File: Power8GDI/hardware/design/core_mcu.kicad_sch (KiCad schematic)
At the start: 31 parts, among them J101 SWD 3V3 target reference, U101 STM32F767IIT6, Y101 ASEM1-8.000MHZ-LC-T

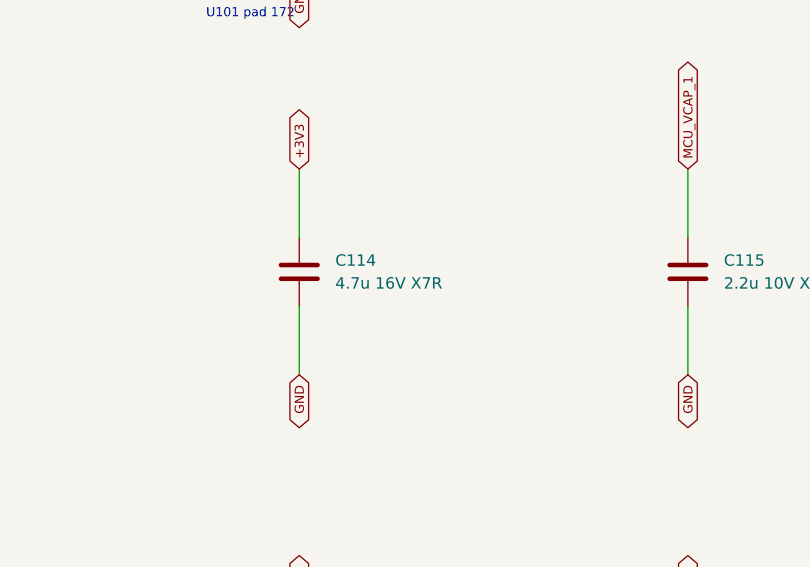
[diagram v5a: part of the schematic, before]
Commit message: Review B58 injector power stage and bind selected GDI6 BOM
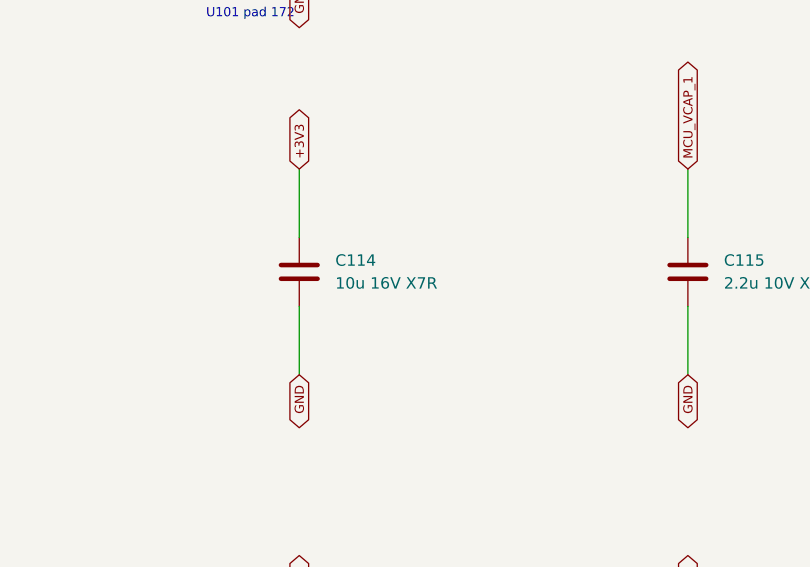
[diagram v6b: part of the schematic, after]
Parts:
- C101, C102, C103, C104, C105, C106, C107, C108, C109, C110, C111, C112, C113, C117, C119, C121, C123, C124: Hardware_Qualification (none) -> BOARD_QUALIFICATION_PENDING; MPN (none) -> C0603C104K5RACTU; Manufacturer (none) -> KEMET; Procurement_Status (none) -> SELECTED_CATALOG_ITEM; Purchase_Released (none) -> false; Selection_Gaps (none) -> []; Selection_ID (none) -> SEL-6bf9727c4e40; Selection_Ratings (none) -> {"capacitance_pf": 100000, "dielectric": "X7R", "rated_volt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; Selection_Source_URLs (none) -> https://search.kemet.com/download/specsheet/C0603C104K5RACTU
- C114: value 4.7u 16V X7R -> 10u 16V X7R; footprint Capacitor_SMD:C_0603_1608Metric -> Capacitor_SMD:C_1206_3216Metric; Design note Package bulk; effective capacitance >=4.7uF after bias/temp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 -> C1206C106K4RACTU candidate; >=4.7uF effective remains a qua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; Hardware_Qualification (none) -> EFFECTIVE_CAPACITANCE_VALIDATION_REQUIRED; MPN (none) -> C1206C106K4RACTU; Manufacturer (none) -> KEMET; Procurement_Status (none) -> SELECTED_CONDITIONAL; Purchase_Released (none) -> false; Selection_Gaps (none) -> ["Nominal10uF alone does not establish required4.7uF effect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; Selection_ID (none) -> SEL-1d8e2bf57acc; Selection_Ratings (none) -> {"capacitance_pf": 10000000, "dc_bias_qualification": "PEND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; Selection_Source_URLs (none) -> https://search.kemet.com/component-documentation/download/s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
- C115, C116: Hardware_Qualification (none) -> BOARD_QUALIFICATION_PENDING; MPN (none) -> C0603C225K8RACTU; Manufacturer (none) -> KEMET; Procurement_Status (none) -> SELECTED_CATALOG_ITEM; Purchase_Released (none) -> false; Selection_Gaps (none) -> ["Required effective capacitance not yet verified with supp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; Selection_ID (none) -> SEL-6e8be3f03886; Selection_Ratings (none) -> {"capacitance_pf": 2200000, "dc_bias_qualification": "PENDI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; Selection_Source_URLs (none) -> https://www.tme.com/us/en-us/details/c0603c225k8rac/mlcc-sm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
- C118, C120, C122: Hardware_Qualification (none) -> BOARD_QUALIFICATION_PENDING; MPN (none) -> C0603C105K3RACTU; Manufacturer (none) -> KEMET; Procurement_Status (none) -> SELECTED_CATALOG_ITEM; Purchase_Released (none) -> false; Selection_Gaps (none) -> []; Selection_ID (none) -> SEL-4bca20b134b8; Selection_Ratings (none) -> {"capacitance_pf": 1000000, "dc_bias_qualification": "PENDI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; Selection_Source_URLs (none) -> https://search.kemet.com/download/specsheet/C0603C105K3RACTU
- C129: Hardware_Qualification (none) -> BOARD_QUALIFICATION_PENDING; MPN (none) -> C0603C103K5RACTU; Manufacturer (none) -> KEMET; Procurement_Status (none) -> SELECTED_CATALOG_ITEM; Purchase_Released (none) -> false; Selection_Gaps (none) -> []; Selection_ID (none) -> SEL-003cf16db818; Selection_Ratings (none) -> {"capacitance_pf": 10000, "dielectric": "X7R", "rated_volta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; Selection_Source_URLs (none) -> https://www.digikey.com/en/products/detail/kemet/C0603C103K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
- J101: Hardware_Qualification (none) -> BOARD_QUALIFICATION_PENDING; MPN (none) -> M50-3500542; Manufacturer (none) -> Harwin; Procurement_Status (none) -> SELECTED_CATALOG_ITEM; Purchase_Released (none) -> false; Selection_Gaps (none) -> []; Selection_ID (none) -> SEL-8ced3adf7c02; Selection_Ratings (none) -> {"current_per_contact_a": 1, "mounting": "through hole", "p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; Selection_Source_URLs (none) -> https://www.digikey.com/en/products/detail/harwin-inc/M50-3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
- R101: Hardware_Qualification (none) -> BOARD_QUALIFICATION_PENDING; MPN (none) -> CRCW06030000Z0EA; Manufacturer (none) -> Vishay; Procurement_Status (none) -> SELECTED_FAMILY_CODE; Purchase_Released (none) -> false; Selection_Gaps (none) -> []; Selection_ID (none) -> SEL-8473f02313b2; Selection_Ratings (none) -> {"aec_q200": true, "current_a": 2, "power_reference_tempera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; Selection_Source_URLs (none) -> https://www.vishay.com/docs/20035/dcrcwe3.pdf
- R102, R103: Hardware_Qualification (none) -> BOARD_QUALIFICATION_PENDING; MPN (none) -> CRCW060310K0FKEA; Manufacturer (none) -> Vishay; Procurement_Status (none) -> SELECTED_FAMILY_CODE; Purchase_Released (none) -> false; Selection_Gaps (none) -> []; Selection_ID (none) -> SEL-9c0806476875; Selection_Ratings (none) -> {"aec_q200": true, "derating": "Use manufacturer power vers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; Selection_Source_URLs (none) -> https://www.vishay.com/docs/20035/dcrcwe3.pdf
- U101: Hardware_Qualification (none) -> PINOUT_RATINGS_AND_DELIVERY_SUFFIX_REVIEW_PENDING; MPN (none) -> STM32F767IIT6; Manufacturer (none) -> STMicroelectronics; Procurement_Status (none) -> REFERENCE_MPN_RETAINED; Purchase_Released (none) -> false; Selection_Gaps (none) -> ["Existing schematic MPN retained. Complete circuit rating/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; Selection_ID (none) -> SEL-8c0220c96a29; Selection_Ratings (none) -> {}; Selection_Source_URLs (none) -> https://www.st.com/en/search.html#q=STM32F767IIT6
- Y101: Hardware_Qualification (none) -> PINOUT_RATINGS_AND_DELIVERY_SUFFIX_REVIEW_PENDING; MPN (none) -> ASEM1-8.000MHZ-LC-T; Manufacturer (none) -> Abracon; Procurement_Status (none) -> REFERENCE_MPN_RETAINED; Purchase_Released (none) -> false; Selection_Gaps (none) -> ["Existing schematic MPN retained. Complete circuit rating/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; Selection_ID (none) -> SEL-4a33baffd848; Selection_Ratings (none) -> {}; Selection_Source_URLs (none) -> https://abracon.com/Oscillators/ASEM.pdf
